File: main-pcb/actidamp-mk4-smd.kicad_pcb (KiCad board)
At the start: 4 copper layers, 119 x 100 mm, 199 parts, among them J101 XLR3, J102 Phono_Ground, J103 PHONO_IN_L, J104 PHONO_IN_R, J105 LINE_OUT_L, J106 LINE_OUT_R, Q201 2SK3320, Q301 2SK3320, Q401 BC846BPN, Q501 BC846BPN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

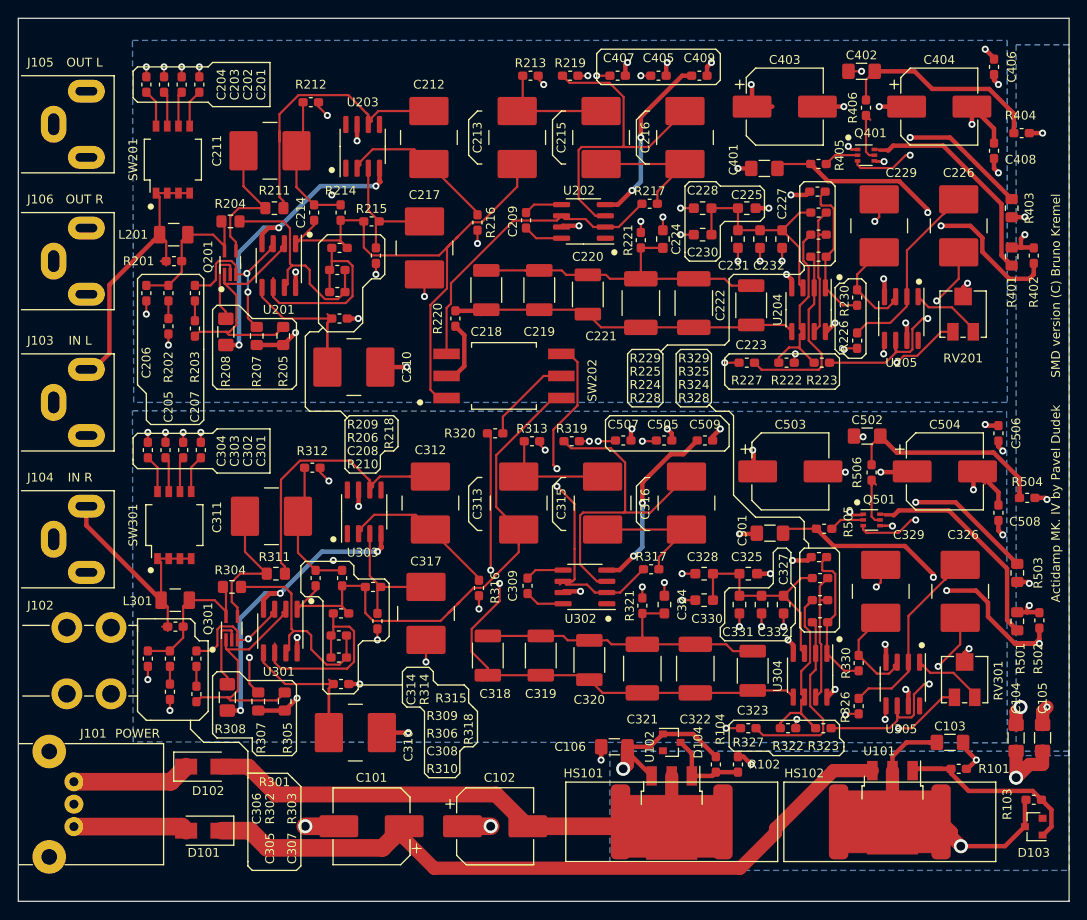
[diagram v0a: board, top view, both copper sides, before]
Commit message: Maek board 100mm wide, fix track too close to the edge
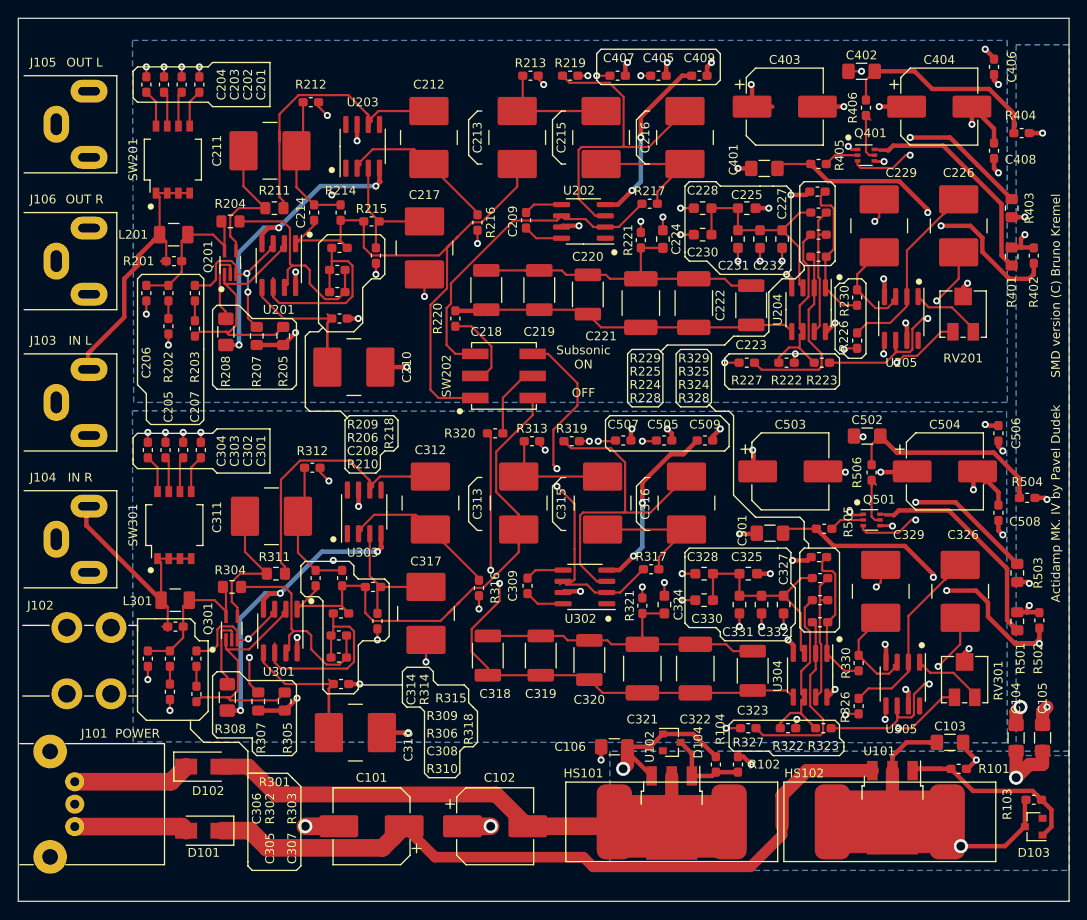
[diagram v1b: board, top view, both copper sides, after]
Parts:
- moved J103 0.30 mm to (90.8, 94.5)
- moved J104 0.30 mm to (90.8, 110.0)
- moved J105 0.30 mm to (90.8, 63.0)
- moved J106 0.30 mm to (90.8, 78.5)
- moved J101 0.10 mm to (94.1, 140.0)
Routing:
- net Net-(C213-Pad2): track 63.0 -> 66.8 mm
- net Net-(R217-Pad1): track 34.6 -> 37.3 mm
- net Net-(R220-Pad1): track 7.40 -> 9.66 mm
- net Net-(R320-Pad1): track 10.4 -> 8.43 mm
- net Net-(C313-Pad2): track 63.5 -> 61.6 mm
- net Net-(C101-Pad1): track 83.2 -> 84.6 mm
- net /left_channel/IN: track 32.3 -> 33.5 mm
- net Net-(R317-Pad1): track 42.5 -> 43.4 mm
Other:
- board text added: "Subsonic ON OFF"
